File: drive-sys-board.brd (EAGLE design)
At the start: 109.2 x 48.3 mm, 29 parts, among them J2 APP_2POS_CONFIG12V_HORIZ, U1 OKI-78SR-5/1.5-W36HC, U2 MAX232, U3 MAX232, U4 MAX232

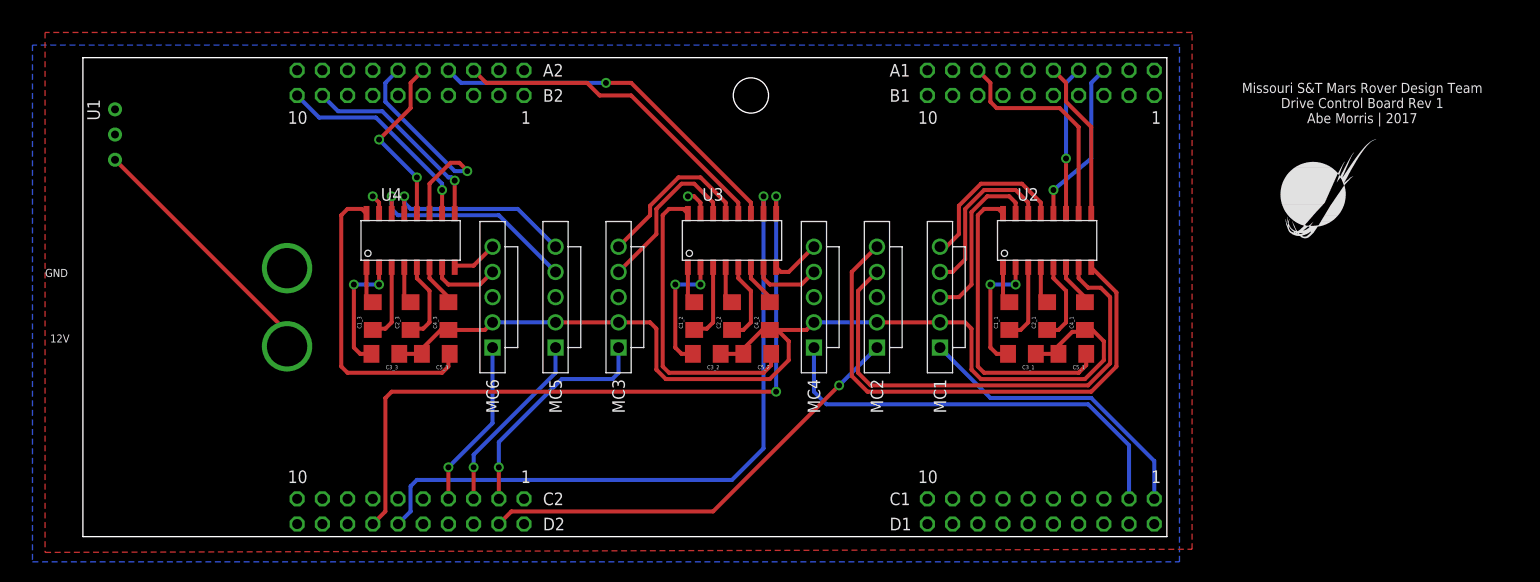
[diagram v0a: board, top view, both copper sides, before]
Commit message: Updated board label
Added my name and the year
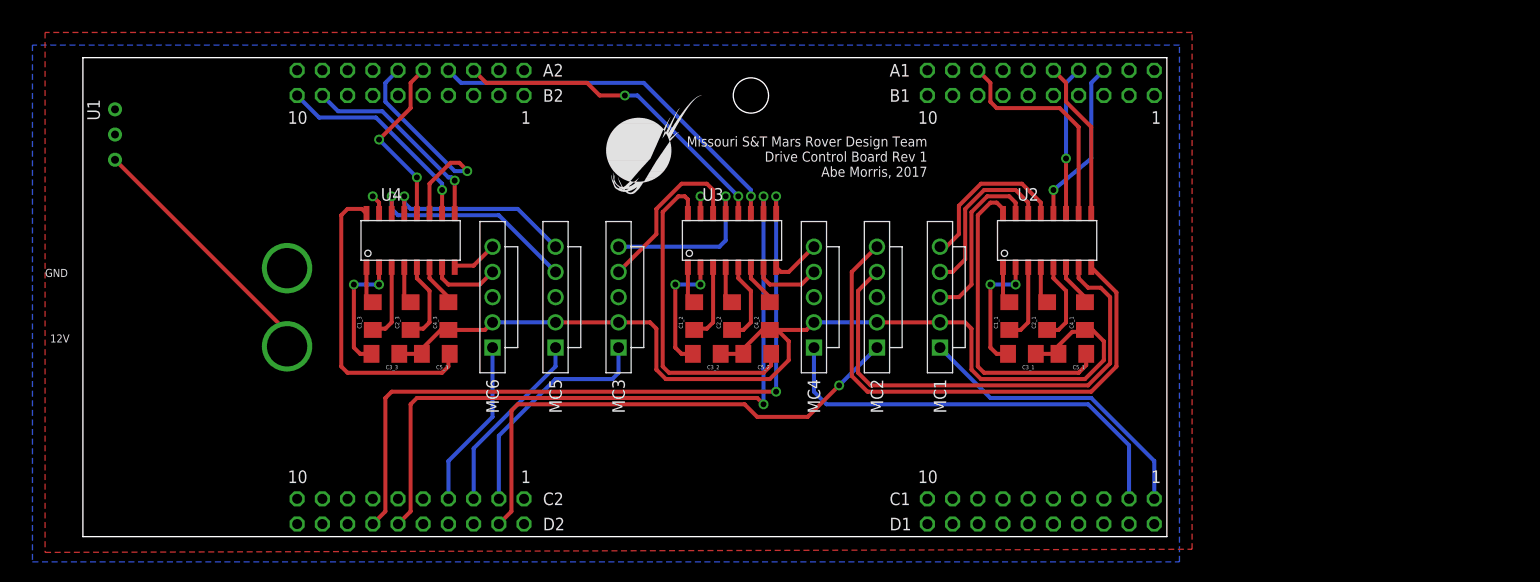
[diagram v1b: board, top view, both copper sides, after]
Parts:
- moved U$2 68.1 mm to (52.7, 33.7)
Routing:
- net PWM_2: track 45.5 -> 52.5 mm
- net TX_4: track 68.6 -> 71.4 mm, vias 1 -> 2
- net N$17: track 30.9 -> 33.0 mm
- net GND: track 22.1 -> 21.2 mm
- net N$33: track 16.4 -> 17.2 mm, vias 0 -> 1
- net N$10: track 30.9 -> 31.7 mm
- net TX_3: track 37.1 -> 37.9 mm
- net N$32: track 16.6 -> 17.3 mm
- net RX_3: track 33.3 -> 33.7 mm, vias 0 -> 2
- net PWM_3: track 23.2 -> 23.6 mm, vias 1 -> 0
- net PWM_5: vias 1 -> 0
- net PWM_6: vias 1 -> 0
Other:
- board text added: "Missouri S&T Mars Rover Design Team Drive Control Board Rev 1 Abe Morris, 2017"
- board text removed: "Missouri S&T Mars Rover Design Team Drive Control Board Rev 1 Abe Morris | 2017"

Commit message: Made slight changes to prepare for board review
- Added decoupling capacitors to OKI
- Replaced VCC supply symbol with +5V
- Disconnected +5V from capacitors (let them connect to +5V plane)
- Swap connectors 3 and 4 to create progression from right to left
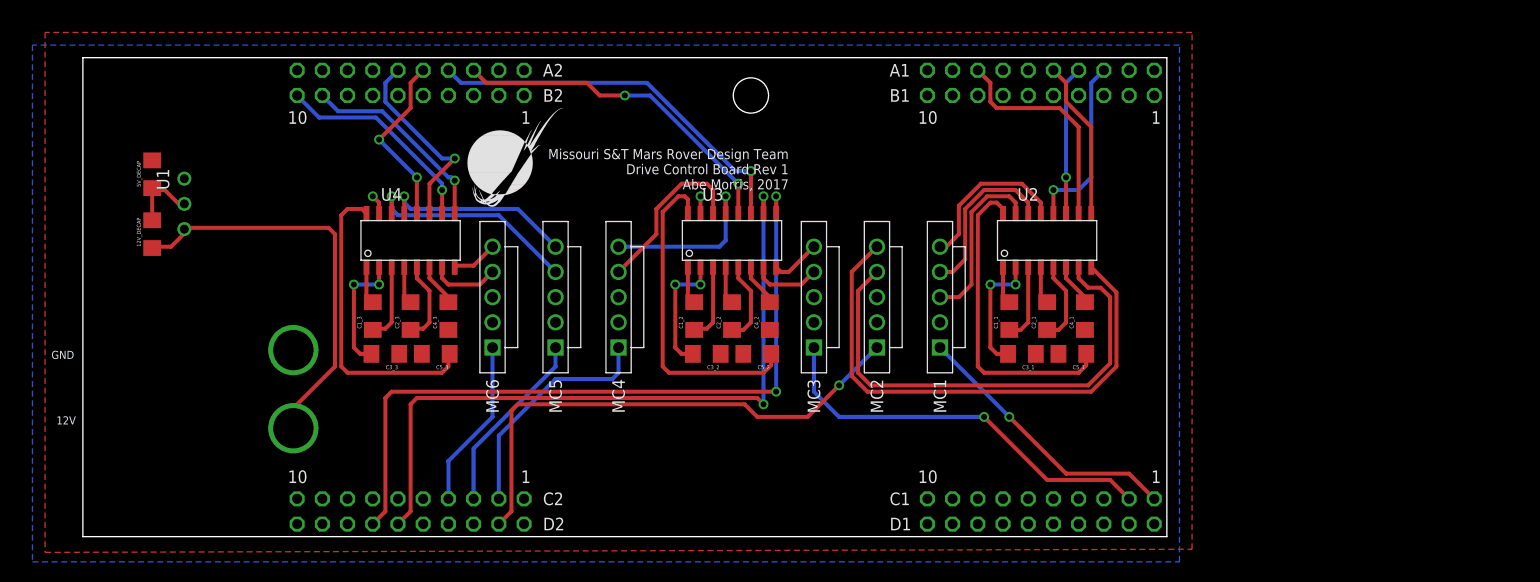
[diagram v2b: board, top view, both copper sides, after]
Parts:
- added 12V_DECAP, 5V_DECAP: 10uF, SparkFun-Capacitors:1206
- moved MC3 19.7 mm to (73.7, 24.1)
- moved MC4 19.7 mm to (54.0, 24.1)
- moved U$2 14.0 mm to (38.7, 32.4)
- moved U1 9.88 mm to (10.2, 31.0)
- moved J2 8.28 mm to (-6.99, 6.99)
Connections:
- removed net VCC: C3_1.1, C3_2.1, C3_3.1, C4_1.1, C4_2.1, C4_3.1, C5_1.2, C5_2.2, C5_3.2, MC1.2, MC2.2, MC3.2, MC4.2, MC5.2, MC6.2
- net +5V: now also 5V_DECAP.2, C3_1.1, C3_2.1, C3_3.1, C4_1.1, C4_2.1, C4_3.1, C5_1.2, C5_2.2, C5_3.2, MC1.2, MC2.2, MC3.2, MC4.2, MC5.2, MC6.2
- net GND: now also 12V_DECAP.2, 5V_DECAP.1
- net N$30: now also MC3.5; no longer MC4.5
- net N$31: now also MC3.4; no longer MC4.4
- net N$32: now also MC4.4; no longer MC3.4
- net N$33: now also MC4.5; no longer MC3.5
- net N$5: now also 12V_DECAP.1
- net PWM_3: now also U$1.PF2; no longer U$1.PK4
- net PWM_4: now also U$1.PK4; no longer U$1.PF2
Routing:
- net VCC: track 107.2 -> 0.00 mm
- net PWM_4: track 43.8 -> 23.6 mm
- net PWM_3: track 23.6 -> 40.7 mm, vias 0 -> 1
- net N$5: track 26.0 -> 41.1 mm
- net GND: track 21.2 -> 28.4 mm
- net TX_5: track 23.0 -> 19.7 mm
- net PWM_1: track 30.1 -> 27.9 mm, vias 0 -> 1
- net RX_1: track 16.8 -> 18.0 mm
- net TX_3: track 37.9 -> 39.0 mm
- net RX_3: track 33.7 -> 34.4 mm

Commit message: Made changes from Drive Board Review 2
- Widened SL Connector Spacing
- Set all MAX232 Capacitors to 1uF, as shown in MAX232 datasheet
- Changed all capacitors from 1206 to 0805
- Increased silkscreen label size
- Added labels for motor position (ex: Front Left, Middle Left, etc)
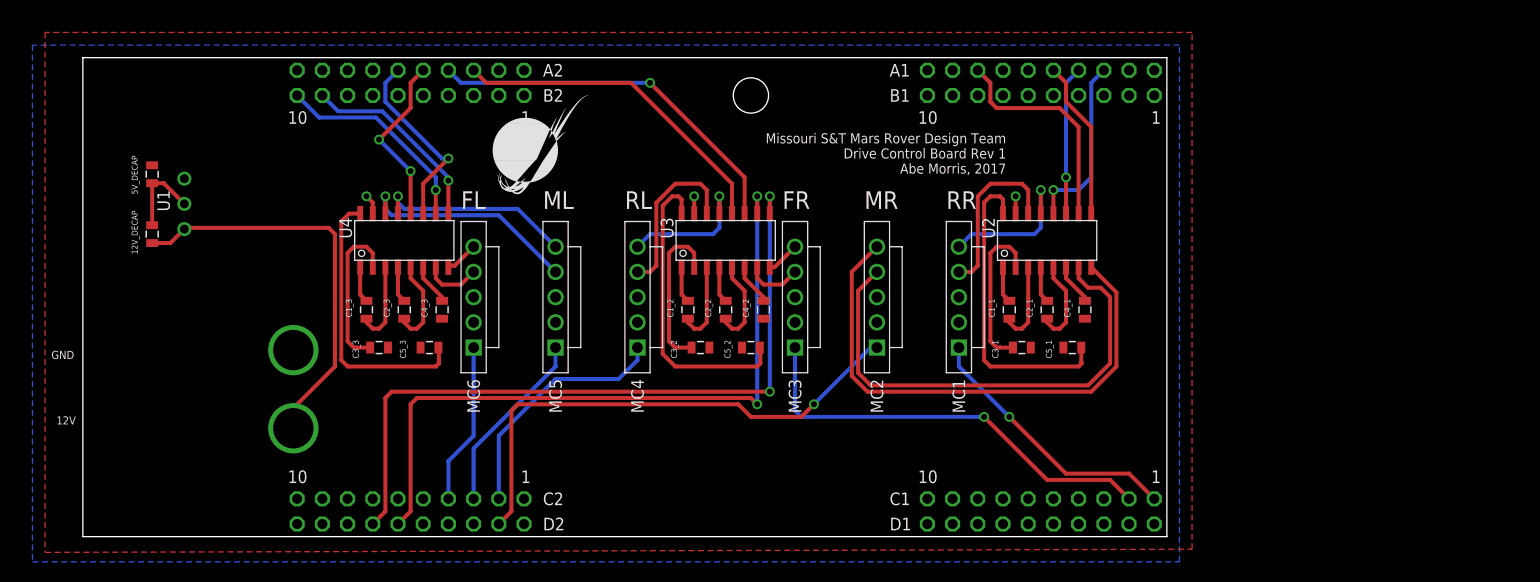
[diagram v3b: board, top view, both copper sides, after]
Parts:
- 12V_DECAP, 5V_DECAP: device SparkFun-Capacitors:1206 -> SparkFun-Capacitors:0805
- C1_1, C1_2, C1_3: value .047uF -> 1uF; device SparkFun-Capacitors:1206 -> SparkFun-Capacitors:0805
- C2_1, C2_2, C2_3, C3_1, C3_2, C3_3, C4_1, C4_2, C4_3: value .33uF -> 1uF; device SparkFun-Capacitors:1206 -> SparkFun-Capacitors:0805
- C5_1, C5_2, C5_3: value .1uF -> 1uF; device SparkFun-Capacitors:1206 -> SparkFun-Capacitors:0805
- moved U$2 2.84 mm to (41.3, 33.7)
- moved MC1 1.91 mm to (88.3, 24.1)
- moved MC3 1.91 mm to (71.8, 24.1)
- moved MC4 1.91 mm to (55.9, 24.1)
- moved MC6 1.91 mm to (39.4, 24.1)
- moved C3_2 0.90 mm to (62.2, 19.1)
- moved C5_3 0.90 mm to (34.9, 19.1)
- moved C3_3 0.90 mm to (29.8, 19.1)
- moved C2_2 0.90 mm to (64.8, 22.9)
- moved C2_3 0.90 mm to (32.4, 22.9)
- moved C4_2 0.90 mm to (68.6, 22.9)
- moved C1_3 0.90 mm to (28.6, 22.9)
- moved C1_2 0.90 mm to (61.0, 22.9)
- moved C4_3 0.90 mm to (36.2, 22.9)
- moved C5_2 0.90 mm to (67.3, 19.1)
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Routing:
- net GND: track 28.4 -> 13.8 mm, vias 2 -> 3
- net N$33: track 17.2 -> 14.0 mm
- net N$21: track 12.7 -> 15.9 mm, vias 2 -> 0
- net N$8: track 12.7 -> 15.9 mm, vias 2 -> 0
- net N$14: track 12.7 -> 15.9 mm, vias 2 -> 0
- net PWM_3: track 40.7 -> 43.7 mm
- net N$24: track 30.9 -> 28.1 mm
- net N$17: track 33.0 -> 31.1 mm
- net N$30: track 5.06 -> 3.40 mm
- net N$28: track 6.98 -> 5.71 mm
- net N$31: track 6.98 -> 5.71 mm
- net N$27: track 4.67 -> 3.40 mm
- net PWM_4: track 23.6 -> 24.7 mm
- net N$37: track 16.4 -> 15.2 mm, vias 0 -> 1
- net TX_3: track 39.0 -> 38.0 mm
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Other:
- board text added: "FL"
- board text added: "FR"
- board text added: "ML"
- board text added: "MR"
- board text added: "RL"
- board text added: "RR"

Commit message: Flipped the silkscreen for the 5Pin SLs
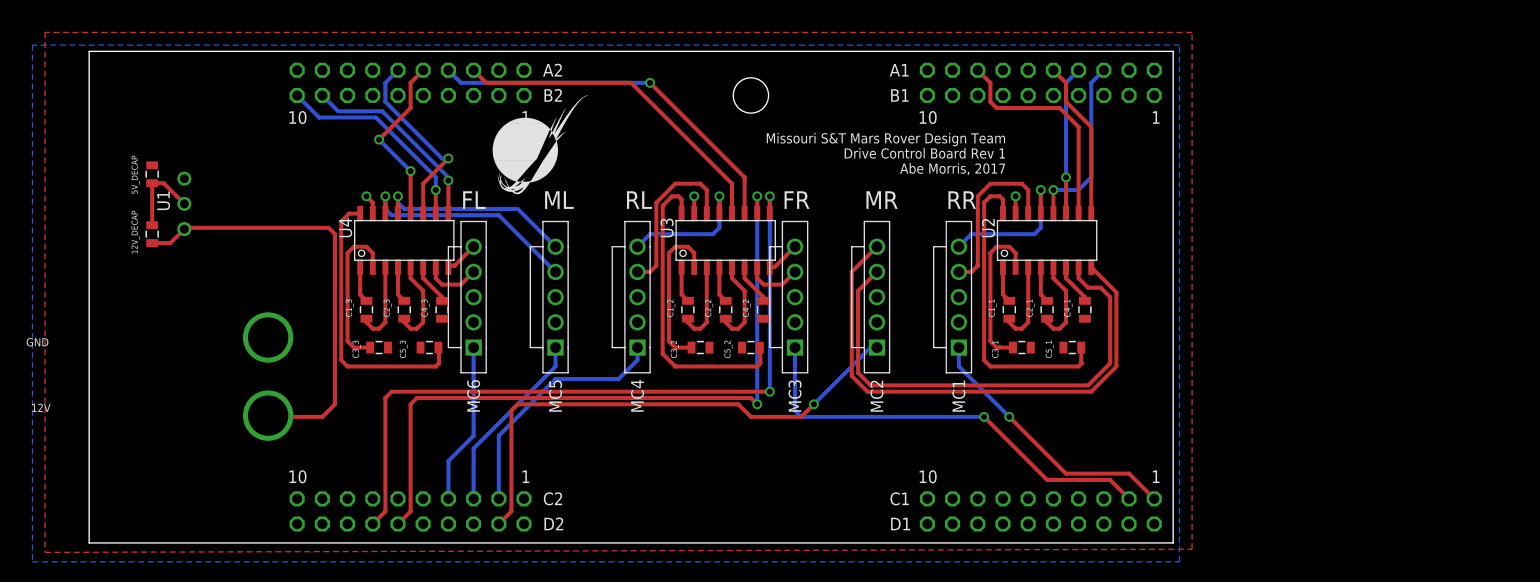
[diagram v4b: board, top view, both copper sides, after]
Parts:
- moved J2 2.84 mm to (-9.53, 8.26)
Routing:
- net N$5: track 40.6 -> 43.8 mm
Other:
- board size 109.2 x 48.3 mm -> 109.2 x 49.5 mm
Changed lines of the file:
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@@
 <board>
 <plain>
-<wire x1="0" y1="0" x2="109.22" y2="0" width="0" layer="20"/>
-<wire x1="109.22" y1="0" x2="109.22" y2="48.26" width="0" layer="20"/>
-<wire x1="109.22" y1="48.26" x2="0" y2="48.26" width="0" layer="20"/>
-<wire x1="0" y1="48.26" x2="0" y2="0" width="0" layer="20"/>
+<wire x1="0.635" y1="-0.635" x2="109.855" y2="-0.635" width="0" layer="20"/>
+<wire x1="109.855" y1="-0.635" x2="109.855" y2="48.895" width="0" layer="20"/>
+<wire x1="109.855" y1="48.895" x2="0.635" y2="48.895" width="0" layer="20"/>
+<wire x1="0.635" y1="48.895" x2="0.635" y2="-0.635" width="0" layer="20"/>
 <text x="93.0275" y="40.64" size="1.016" layer="21" font="vector" rot="R180">Missouri S&amp;T Mars Rover Design Team
 Drive Control Board Rev 1
@@
 <attribute name="NAME" x="8.763" y="32.766" size="1.27" layer="25" font="vector" rot="R90"/>
 </element>
-<element name="J2" library="MRDT-Connectors" package="APP45_12V_HORIZ_CONFIG" value="APP_2POS_CONFIG12V_HORIZ" x="-6.985" y="6.985">
-<attribute name="COLOR1" value="YELLOW" x="-6.985" y="6.985" size="1.778" layer="27" display="off"/>
-<attribute name="COLOR2" value="BLACK" x="-6.985" y="6.985" size="1.778" layer="27" display="off"/>
+<element name="J2" library="MRDT-Connectors" package="APP45_12V_HORIZ_CONFIG" value="APP_2POS_CONFIG12V_HORIZ" x="-9.525" y="8.255">
+<attribute name="COLOR1" value="YELLOW" x="-9.525" y="8.255" size="1.778" layer="27" display="off"/>
+<attribute name="COLOR2" value="BLACK" x="-9.525" y="8.255" size="1.778" layer="27" display="off"/>
 </element>
 <element name="U2" library="MRDT-ICs" package="SOIC16" value="MAX232" x="97.155" y="29.845" smashed="yes">
@@
 <contactref element="12V_DECAP" pad="1"/>
 <contactref element="U1" pad="1"/>
-<wire x1="21.209" y1="10.922" x2="21.209" y2="12.954" width="0.4064" layer="1"/>
-<wire x1="21.209" y1="12.954" x2="25.4" y2="17.145" width="0.4064" layer="1"/>
-<wire x1="25.4" y1="17.145" x2="25.4" y2="30.48" width="0.4064" layer="1"/>
+<wire x1="25.4" y1="13.335" x2="25.4" y2="30.48" width="0.4064" layer="1"/>
 <wire x1="10.3505" y1="31.115" x2="10.2235" y2="30.988" width="0.4064" layer="1"/>
 <wire x1="10.2235" y1="30.988" x2="8.8155" y2="29.58" width="0.4064" layer="1"/>
@@
 <wire x1="10.3505" y1="31.115" x2="24.765" y2="31.115" width="0.4064" layer="1"/>
 <wire x1="24.765" y1="31.115" x2="25.4" y2="30.48" width="0.4064" layer="1"/>
+<wire x1="25.4" y1="13.335" x2="24.13" y2="12.065" width="0.4064" layer="1"/>
+<wire x1="24.13" y1="12.065" x2="18.796" y2="12.065" width="0.4064" layer="1"/>
+<wire x1="18.796" y1="12.065" x2="18.669" y2="12.192" width="0.4064" layer="1"/>
 </signal>
 <signal name="N$3">

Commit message: Adjusted positions of several board components
- Repositioned OKI to allow for more room
- Shifted the two leftmost MAX232s to the left
- Shifted SL Connectors to be evenly spaced between MAX232s
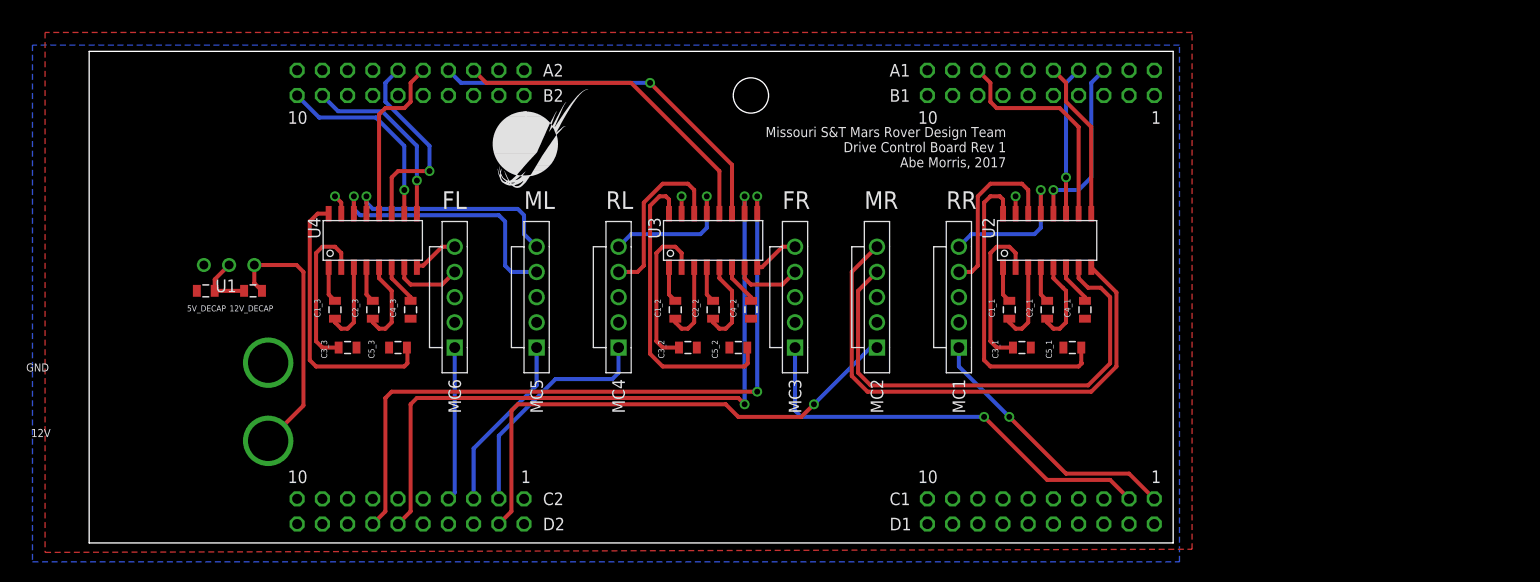
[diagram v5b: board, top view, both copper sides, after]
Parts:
- moved 5V_DECAP 12.9 mm to (12.4, 24.8), turned to 180 degrees
- moved 12V_DECAP 11.7 mm to (17.1, 24.8), turned to 180 degrees
- moved U1 7.92 mm to (17.3, 27.4), turned to 0 degrees
- moved C1_3 3.18 mm to (25.4, 22.9)
- moved C2_3 3.17 mm to (29.2, 22.9)
- moved C3_3 3.17 mm to (26.7, 19.1)
- moved C4_3 3.17 mm to (33.0, 22.9)
- moved C5_3 3.17 mm to (31.8, 19.1)
- moved U4 3.17 mm to (29.2, 29.8)
- moved J2 2.54 mm to (-9.53, 5.71)
- moved MC4 1.91 mm to (54.0, 24.1)
- moved MC5 1.91 mm to (45.7, 24.1)
- moved MC6 1.90 mm to (37.5, 24.1)
- moved C1_2 1.27 mm to (59.7, 22.9)
- moved C2_2 1.27 mm to (63.5, 22.9)
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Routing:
- net N$5: track 43.8 -> 26.7 mm
- net N$26: track 22.8 -> 26.7 mm
- net N$29: track 20.1 -> 22.5 mm
- net GND: track 13.8 -> 11.7 mm
- net TX_6: track 21.0 -> 19.7 mm
- net N$30: track 3.40 -> 4.67 mm
- net RX_4: track 73.7 -> 72.4 mm
- net N$28: track 5.71 -> 6.98 mm
- net N$27: track 3.40 -> 4.67 mm
- net N$31: track 5.71 -> 6.98 mm
- net TX_4: track 70.7 -> 69.5 mm
- net TX_5: track 19.0 -> 20.3 mm
- net PWM_4: track 24.7 -> 23.6 mm
- net RX_6: track 19.8 -> 18.8 mm
- net PWM_5: track 18.7 -> 17.9 mm
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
